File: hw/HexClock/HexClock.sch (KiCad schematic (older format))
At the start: 30 parts, among them J1 Screw_Terminal_01x02, Q1 2N3906, Q2 2N3906, Q3 2N3906, Q4 2N3906, SW1 SW_Push, SW2 SW_Push, SW3 SW_Push, U1 DS1307+, Y1 32.768 KHz

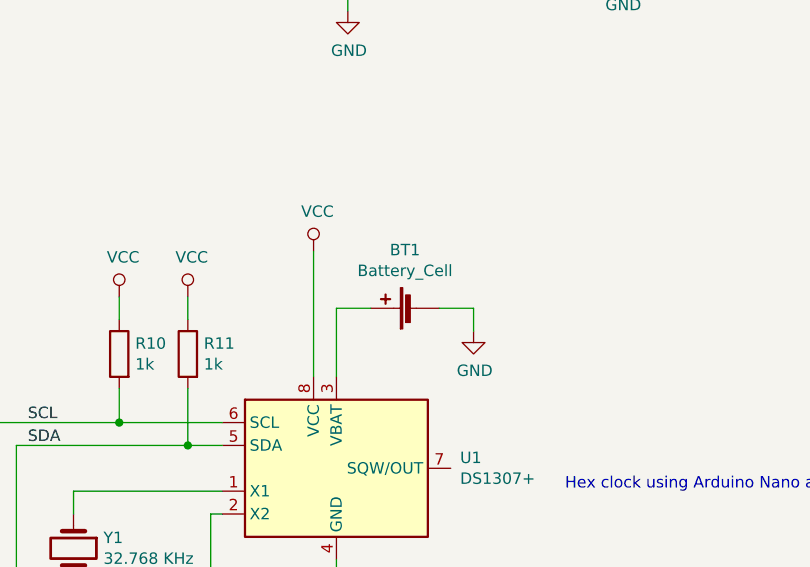
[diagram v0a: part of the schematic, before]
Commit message: tie DS1307 VBAT to ground
I could not get the DS1307 to work correctly with
the battery connected.
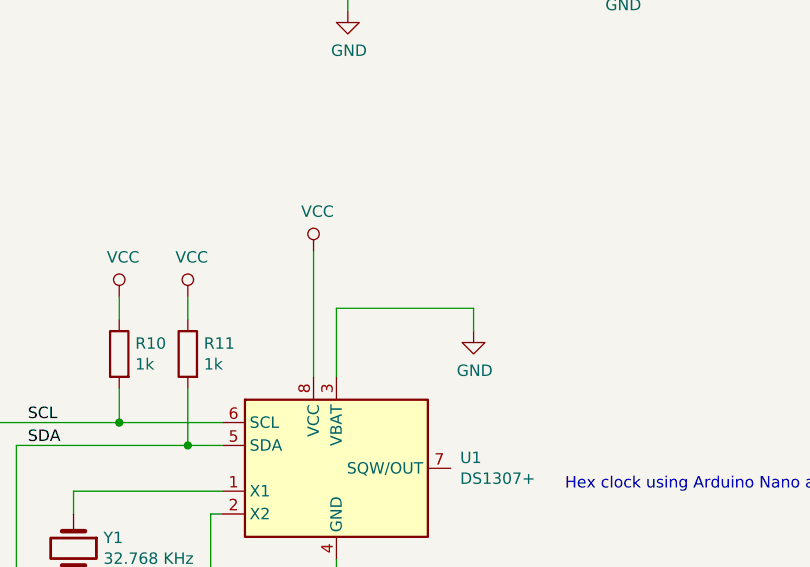
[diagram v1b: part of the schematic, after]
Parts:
- removed BT1: Battery_Cell, symbol device:Battery_Cell
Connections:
- wire segments 157 -> 156
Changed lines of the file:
@@
 	1    0    0    -1
 $EndComp
-$Comp
-L device:Battery_Cell BT1
-U 1 1 5CC3142E
-P 5700 6150
-F 0 "BT1" V 5955 6200 50  0000 C CNN
-F 1 "Battery_Cell" V 5864 6200 50  0000 C CNN
-F 2 "" V 5700 6210 50  0001 C CNN
-F 3 "" V 5700 6210 50  0001 C CNN
-	1    5700 6150
-	0    -1   -1   0
-$EndComp
-Wire Wire Line
-	5500 6150 5350 6150
 Wire Wire Line
 	5350 6150 5350 6450
-Wire Wire Line
-	5800 6150 5950 6150
 Wire Wire Line
 	5950 6150 5950 6250
@@
 Wire Wire Line
 	3250 4000 3500 4000
+Connection ~ 3500 4000
+Wire Wire Line
+	3500 4000 3500 3850
+Wire Wire Line
+	5350 6150 5950 6150
 Wire Bus Line
 	950  3150 8300 3150
@@
 Wire Bus Line
 	8400 2000 8400 3050
-Connection ~ 3500 4000
-Wire Wire Line
-	3500 4000 3500 3850
 $EndSCHEMATC
